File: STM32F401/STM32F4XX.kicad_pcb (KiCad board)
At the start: 2 copper layers, 61 x 68.6 mm, 32 parts, among them J1 DEBUG UART, J2 Conn_02x16_Counter_Clockwise, J3 USB_B_Mini, J4 Conn_02x16_Counter_Clockwise, J5 JTAG SWDIO SWCLK, SW1 ~RESET, U1 STM32F401RCTx, U2 LM1117-3.3, Y1 8MHz

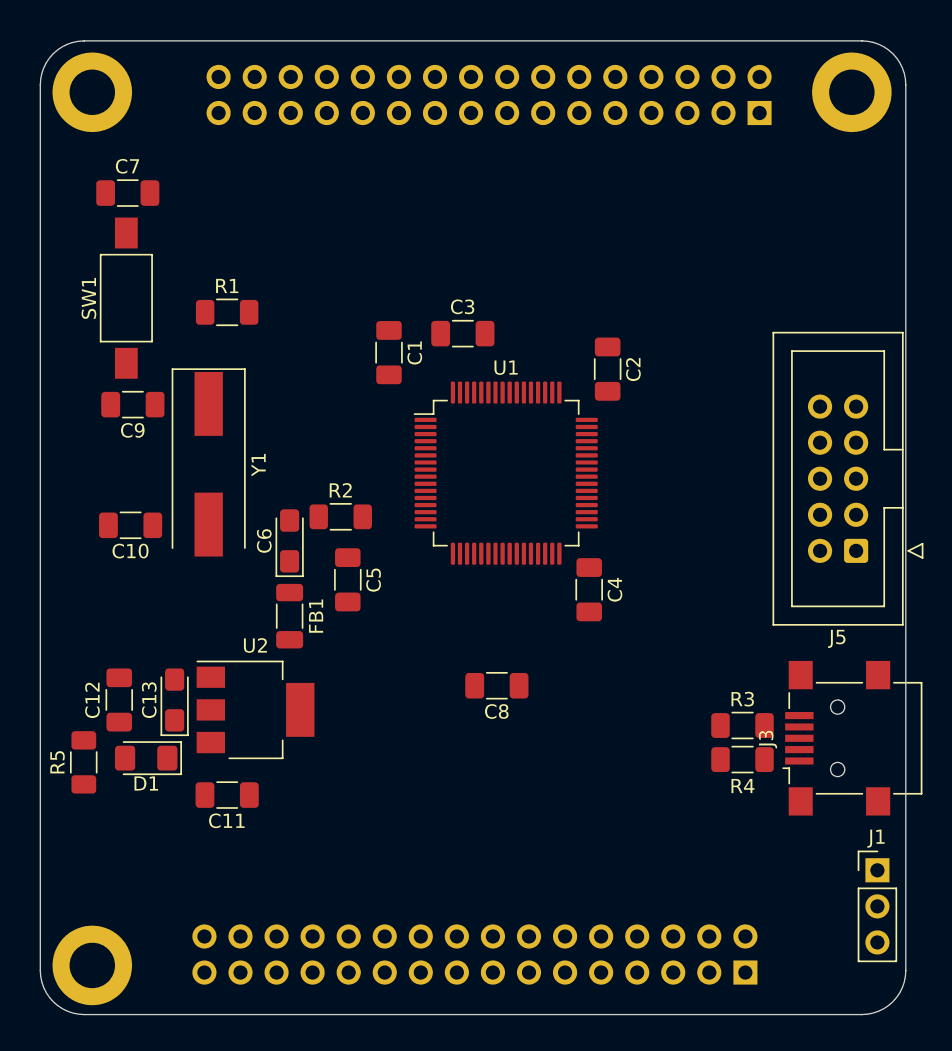
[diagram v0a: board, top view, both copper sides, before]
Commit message: Modified for JLCPCB production and added some silkscreens
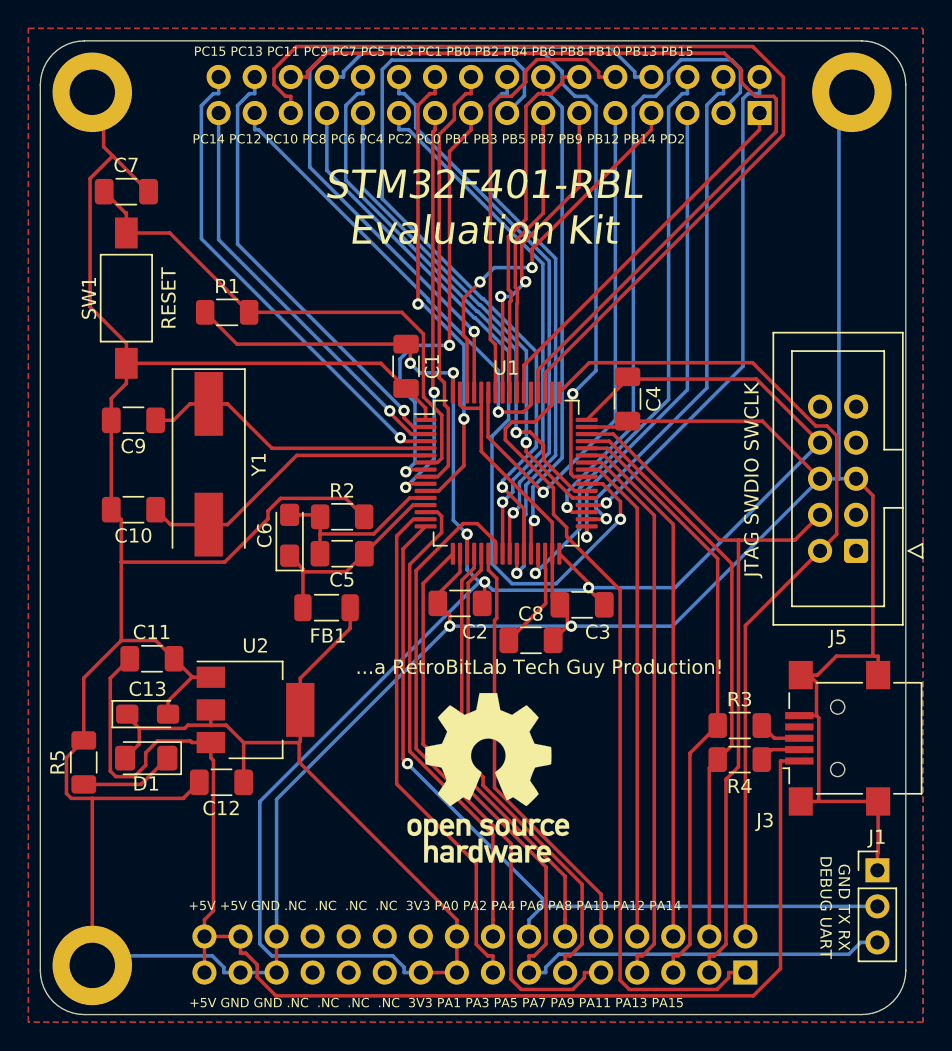
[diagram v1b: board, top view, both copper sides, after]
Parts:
- added LOGO2: OSH, Symbol:OSHW-Logo_11.4x12mm_SilkScreen, F.Cu at (148.4, 107.8)
- C10, C9: value 8pF -> 22pF
- C13: value 20uF -> 10uF; footprint Capacitor_Tantalum_SMD:CP_EIA-3216-18_Kemet-A_Pad1.58x1.35mm_HandSolder -> Capacitor_Tantalum_SMD:CP_EIA-3216-12_Kemet-S_Pad1.58x1.35mm_HandSolder
- D1: value LED -> RED
- U1: value STM32F401RCTx -> STM32F401RCT6
- moved C3 20.9 mm to (155.0, 95.6), turned to 180 degrees
- moved C2 19.5 mm to (146.4, 95.5), turned to 180 degrees
- moved C4 13.7 mm to (158.2, 81.1)
- moved C11 11.0 mm to (124.7, 99.4), turned to 0 degrees
- moved C12 9.25 mm to (129.6, 108.1), turned to 180 degrees
- moved C8 4.00 mm to (151.4, 98.1), turned to 0 degrees
- moved FB1 2.67 mm to (137.0, 95.8), turned to 0 degrees
- moved C13 2.15 mm to (124.4, 103.3), turned to 0 degrees
- moved C5 1.88 mm to (138.1, 92.0), turned to 180 degrees
- moved C1 1.54 mm to (142.6, 78.8)
- moved C10 1.12 mm to (123.4, 88.9)
- moved C9 1.10 mm to (123.4, 82.6)
- moved C6 0.40 mm to (134.4, 90.7)
- moved R3 0.20 mm to (166.1, 104.1)
- moved R4 0.20 mm to (166.1, 106.5)
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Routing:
- net GND: track 0.00 -> 325.5 mm, vias 0 -> 2
- net +3V3: track 0.00 -> 191.0 mm, vias 0 -> 5
- net VCC: track 0.00 -> 94.1 mm
- net C10: track 0.00 -> 70.4 mm
- net C11: track 0.00 -> 64.6 mm
- net A14: track 0.00 -> 60.5 mm
- net A3: track 0.00 -> 60.3 mm
- net A2: track 0.00 -> 57.6 mm, vias 0 -> 1
- net A15: track 0.00 -> 56.9 mm
- net B1: track 0.00 -> 54.4 mm, vias 0 -> 1
- net B8: track 0.00 -> 53.3 mm, vias 0 -> 1
- net C8: track 0.00 -> 53.2 mm, vias 0 -> 1
- net A13: track 0.00 -> 51.8 mm
- net C9: track 0.00 -> 49.7 mm, vias 0 -> 1
- net A7: track 0.00 -> 47.2 mm
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- added copper zone on B.Cu, net GND
- added copper zone on F.Cu, net GND
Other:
- board text added: "+5V +5V GND .NC .NC .NC .NC 3V3 PA0 PA2 PA4 PA6 PA8 PA10 PA12 PA14"
- board text added: "+5V GND GND .NC .NC .NC .NC 3V3 PA1 PA3 PA5 PA7 PA9 PA11 PA13 PA15"
- board text added: "...a RetroBitLab Tech Guy Production!"
- board text added: "GND TX RX DEBUG UART"
- board text added: "JTAG SWDIO SWCLK"
- board text added: "PC14 PC12 PC10 PC8 PC6 PC4 PC2 PC0 PB1 PB3 PB5 PB7 PB9 PB12 PB14 PD2"
- board text added: "PC15 PC13 PC11 PC9 PC7 PC5 PC3 PC1 PB0 PB2 PB4 PB6 PB8 PB10 PB13 PB15"
- board text added: "RESET"
- board text added: "STM32F401-RBL Evaluation Kit"
- board text added: "https://github.com/gianlucarenzi/STM32F4XX/STM32F401"
- board text added: "in memoriam A.S. - G.D."

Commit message: Added KiCAD loAdded KiCAD logo on back silkscreen
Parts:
- added LOGO2: designed with KiCAD, Symbol:KiCad-Logo2_6mm_SilkScreen, B.Cu at (148.1, 108.4)
- renumbered LOGO2 to LOGO1

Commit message: Updated without silkscreen data on back. Only strings
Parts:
- LOGO2: moved to F.Cu
- moved LOGO2 44.9 mm to (167.2, 67.8), turned to 0 degrees

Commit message: Updated footprint for RESET switch. It will a 7.3x3.9x2.5 mm like a Wuerth 434121025816
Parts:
- SW1: footprint RetroBitLab:SW_SPST_FSMSM_3D -> RetroBitLab:SPST-7.3x3.9x2.5-WUERTH-434121025816
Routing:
- net Net-(C7-Pad1): track 38.0 -> 39.4 mm
